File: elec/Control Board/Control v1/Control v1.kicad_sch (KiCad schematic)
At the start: 26 parts, among them J1 DB9_Female_MountingHoles, J10 Screw_Terminal_01x02, J11 Screw_Terminal_01x02, J12 Screw_Terminal_01x02, J2 Conn_01x08, J3 Conn_01x08, J4 Conn_01x08, J5 Conn_01x08, J6 Conn_01x08, J7 Conn_02x18_Odd_Even, J8 Conn_01x10_MountingPin, J9 Conn_02x12_Odd_Even

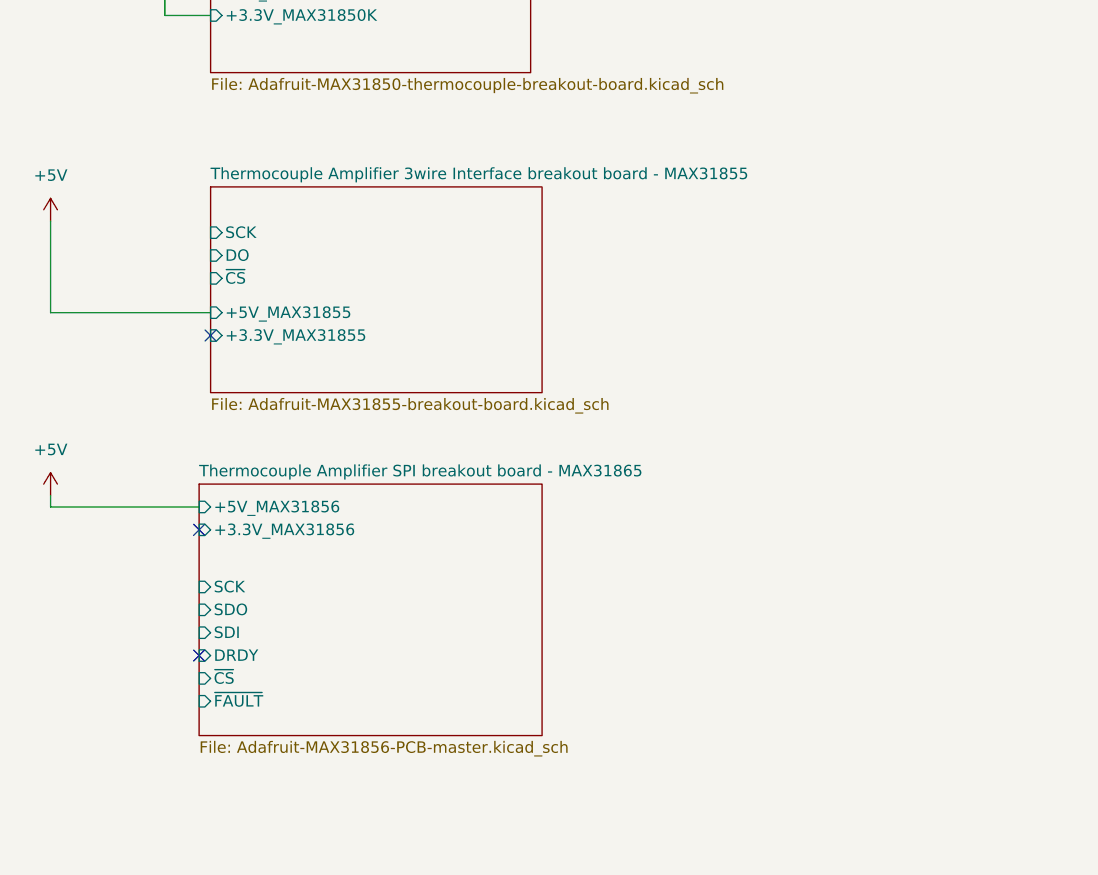
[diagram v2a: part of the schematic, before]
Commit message: Update schematic for MCP9600 I2C thermocouple.
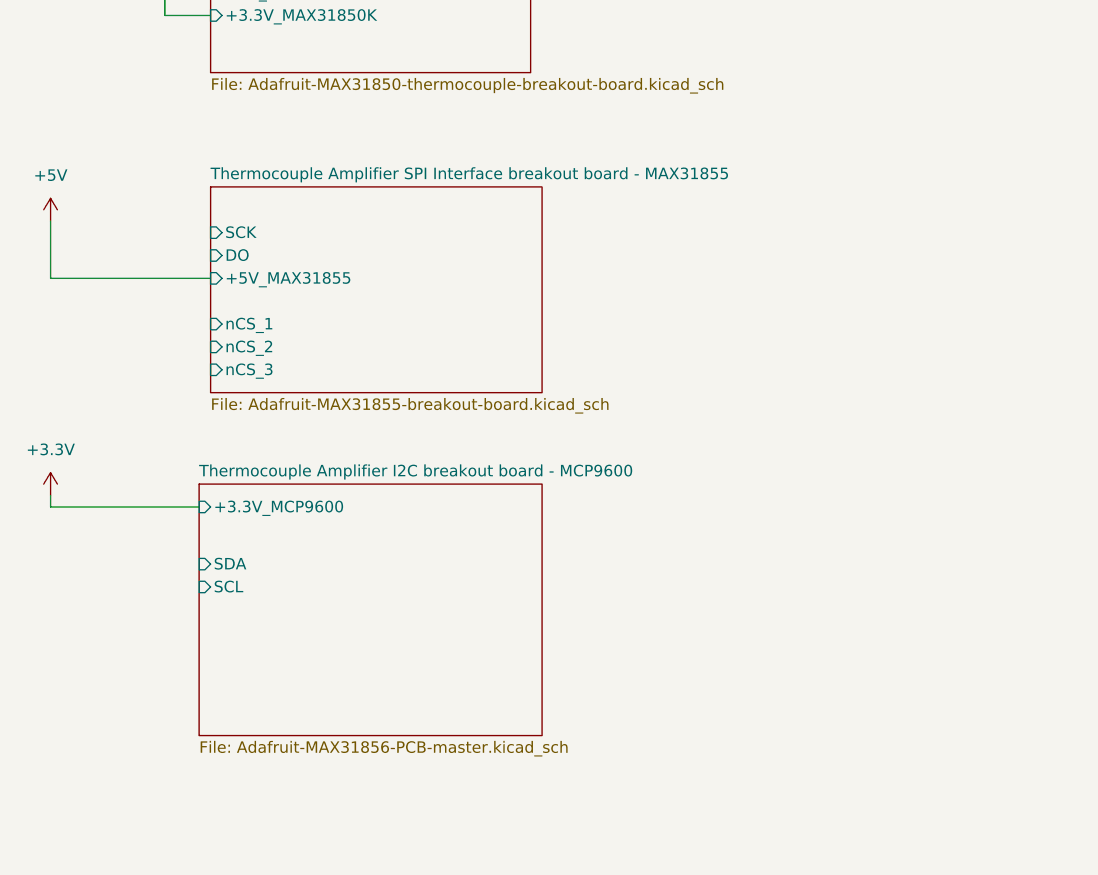
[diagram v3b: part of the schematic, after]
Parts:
- H1, H2, H3, H4, H5: footprint GeneralPurposeAlarmDevicePCB:MountingHole_3.5mm_Pad_Via -> PubInv_KiCad_PCB:MountingHole_3.5mm_Pad_Via
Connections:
- no-connect marks 9 -> 6
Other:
- sheet Thermocouple Amplifier 3wire Interface breakout board - MAX31855  renamed Thermocouple Amplifier SPI Interface breakout board - MAX31855 
- sheet Thermocouple Amplifier SPI breakout board - MAX31865 renamed Thermocouple Amplifier I2C breakout board - MCP9600
- sheet Thermocouple Amplifier I2C breakout board - MCP9600 ports: added +3.3V_MCP9600, SCL, SDA; removed +3.3V_MAX31856, +5V_MAX31856, DRDY, SCK, SDI, SDO, ~{CS}, ~{FAULT}
- sheet Thermocouple Amplifier SPI Interface breakout board - MAX31855  ports: added nCS_1, nCS_2, nCS_3; removed +3.3V_MAX31855, ~{CS}
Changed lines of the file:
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@@
   )
   (no_connect (at 29.21 166.37))
-  (no_connect (at 34.29 215.9))
   (no_connect (at 29.21 163.83))
   (no_connect (at 152.4 171.45))
   (no_connect (at 29.21 168.91))
-  (no_connect (at 33.02 251.46))
   (no_connect (at 29.21 161.29))
   (no_connect (at 29.21 171.45))
-  (no_connect (at 33.02 237.49))
   (wire (pts (xy 250.19 138.43) (xy 250.19 143.51))
     (stroke (width 0) (type default))
@@
     (stroke (width 0) (type default))
   )
-  (wire (pts (xy 34.29 213.36) (xy 16.51 213.36))
+  (wire (pts (xy 34.29 209.55) (xy 16.51 209.55))
     (stroke (width 0) (type default))
   )
@@
     (stroke (width 0) (type default))
   )
-  (wire (pts (xy 16.51 213.36) (xy 16.51 203.2))
+  (wire (pts (xy 16.51 209.55) (xy 16.51 203.2))
     (stroke (width 0) (type default))
   )
@@
       (effects (font (size 1.27 1.27)) (justify left))
     )
-    (property "Footprint" "GeneralPurposeAlarmDevicePCB:MountingHole_3.5mm_Pad_Via" (at 160.02 260.35 0)
+    (property "Footprint" "PubInv_KiCad_PCB:MountingHole_3.5mm_Pad_Via" (at 160.02 260.35 0)
       (effects (font (size 1.27 1.27)) hide)
     )
@@
       (effects (font (size 1.27 1.27)) (justify left))
     )
-    (property "Footprint" "GeneralPurposeAlarmDevicePCB:MountingHole_3.5mm_Pad_Via" (at 160.02 229.87 0)
+    (property "Footprint" "PubInv_KiCad_PCB:MountingHole_3.5mm_Pad_Via" (at 160.02 229.87 0)
       (effects (font (size 1.27 1.27)) hide)
     )
@@
       (effects (font (size 1.27 1.27)) (justify left))
     )
-    (property "Footprint" "GeneralPurposeAlarmDevicePCB:MountingHole_3.5mm_Pad_Via" (at 160.02 237.49 0)
+    (property "Footprint" "PubInv_KiCad_PCB:MountingHole_3.5mm_Pad_Via" (at 160.02 237.49 0)
       (effects (font (size 1.27 1.27)) hide)
     )
@@
     )
   )
+  (symbol (lib_id "power:+3.3V") (at 16.51 233.68 0) (mirror y) (unit 1)
+    (in_bom yes) (on_board yes) (dnp no) (fields_autoplaced)
+    (property "Reference" "#PWR028" (at 16.51 237.49 0)
+      (effects (font (size 1.27 1.27)) hide)
+    )
+    (property "Value" "+3.3V" (at 16.51 228.6 0)
+      (effects (font (size 1.27 1.27)))
+    )
+    (property "Footprint" "" (at 16.51 233.68 0)
+      (effects (font (size 1.27 1.27)) hide)
+    )
+    (property "Datasheet" "" (at 16.51 233.68 0)
+      (effects (font (size 1.27 1.27)) hide)
+    )
+    (pin "1")
+    (instances
+      (project "Control v1"
+        (path "/c68c9deb-8d4d-42f0-adf8-4d3022f4ee59"
+          (reference "#PWR028") (unit 1)
+        )
+      )
+    )
+  )
   (symbol (lib_id "Connector:Screw_Terminal_01x02") (at 394.97 194.31 0) (unit 1)
     (in_bom yes) (on_board yes) (dnp no) (fields_autoplaced)
@@
       (effects (font (size 1.27 1.27)) (justify left))
     )
-    (property "Footprint" "GeneralPurposeAlarmDevicePCB:MountingHole_3.5mm_Pad_Via" (at 160.02 252.73 0)
+    (property "Footprint" "PubInv_KiCad_PCB:MountingHole_3.5mm_Pad_Via" (at 160.02 252.73 0)
       (effects (font (size 1.27 1.27)) hide)
     )
@@
     )
   )
-  (symbol (lib_id "power:+5V") (at 16.51 233.68 0) (unit 1)
-    (in_bom yes) (on_board yes) (dnp no) (fields_autoplaced)
-    (property "Reference" "#PWR03" (at 16.51 237.49 0)
-      (effects (font (size 1.27 1.27)) hide)
-    )
-    (property "Value" "+5V" (at 16.51 228.6 0)
-      (effects (font (size 1.27 1.27)))
-    )
-    (property "Footprint" "" (at 16.51 233.68 0)
-      (effects (font (size 1.27 1.27)) hide)
-    )
-    (property "Datasheet" "" (at 16.51 233.68 0)
-      (effects (font (size 1.27 1.27)) hide)
-    )
-    (pin "1")
-    (instances
-      (project "Control v1"
-        (path "/c68c9deb-8d4d-42f0-adf8-4d3022f4ee59"
-          (reference "#PWR03") (unit 1)
-        )
-      )
-    )
-  )
   (symbol (lib_id "power:+5V") (at 16.51 203.2 0) (unit 1)
     (in_bom yes) (on_board yes) (dnp no) (fields_autoplaced)
@@
       (effects (font (size 1.27 1.27)) (justify left))
     )
-    (property "Footprint" "GeneralPurposeAlarmDevicePCB:MountingHole_3.5mm_Pad_Via" (at 160.02 245.11 0)
+    (property "Footprint" "PubInv_KiCad_PCB:MountingHole_3.5mm_Pad_Via" (at 160.02 245.11 0)
       (effects (font (size 1.27 1.27)) hide)
     )
@@
     (stroke (width 0.1524) (type solid))
     (fill (color 0 0 0 0.0000))
-    (property "Sheetname" "Thermocouple Amplifier SPI breakout board - MAX31865" (at 33.02 231.6984 0)
+    (property "Sheetname" "Thermocouple Amplifier I2C breakout board - MCP9600" (at 33.02 231.6984 0)
       (effects (font (size 1.27 1.27)) (justify left bottom))
     )
@@
       (effects (font (size 1.27 1.27)) (justify left top))
     )
-    (pin "SCK" input (at 33.02 243.84 180)
+    (pin "SDA" input (at 33.02 241.3 180)
       (effects (font (size 1.27 1.27)) (justify left))
     )
-    (pin "SDO" input (at 33.02 246.38 180)
+    (pin "SCL" input (at 33.02 243.84 180)
       (effects (font (size 1.27 1.27)) (justify left))
     )
-    (pin "SDI" input (at 33.02 248.92 180)
-      (effects (font (size 1.27 1.27)) (justify left))
-    )
-    (pin "DRDY" input (at 33.02 251.46 180)
-      (effects (font (size 1.27 1.27)) (justify left))
-    )
-    (pin "~{CS}" input (at 33.02 254 180)
-      (effects (font (size 1.27 1.27)) (justify left))
-    )
-    (pin "~{FAULT}" input (at 33.02 256.54 180)
-      (effects (font (size 1.27 1.27)) (justify left))
-    )
-    (pin "+5V_MAX31856" input (at 33.02 234.95 180)
-      (effects (font (size 1.27 1.27)) (justify left))
-    )
-    (pin "+3.3V_MAX31856" input (at 33.02 237.49 180)
+    (pin "+3.3V_MCP9600" input (at 33.02 234.95 180)
       (effects (font (size 1.27 1.27)) (justify left))
     )
@@
     (stroke (width 0.1524) (type solid))
     (fill (color 0 0 0 0.0000))
-    (property "Sheetname" "Thermocouple Amplifier 3wire Interface breakout board - MAX31855 " (at 34.29 198.6784 0)
+    (property "Sheetname" "Thermocouple Amplifier SPI Interface breakout board - MAX31855 " (at 34.29 198.6784 0)
       (effects (font (size 1.27 1.27)) (justify left bottom))
     )
@@
       (effects (font (size 1.27 1.27)) (justify left))
     )
-    (pin "~{CS}" input (at 34.29 209.55 180)
+    (pin "+5V_MAX31855" input (at 34.29 209.55 180)
+      (effects (font (size 1.27 1.27)) (justify left))
+    )
+    (pin "nCS_3" input (at 34.29 219.71 180)
       (effects (font (size 1.27 1.27)) (justify left))
     )
-    (pin "+5V_MAX31855" input (at 34.29 213.36 180)
+    (pin "nCS_2" input (at 34.29 217.17 180)
       (effects (font (size 1.27 1.27)) (justify left))
     )
-    (pin "+3.3V_MAX31855" input (at 34.29 215.9 180)
+    (pin "nCS_1" input (at 34.29 214.63 180)
       (effects (font (size 1.27 1.27)) (justify left))
     )

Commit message: Next and place thermocouple boards.
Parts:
- removed J11, J12: Screw_Terminal_01x02, symbol Connector:Screw_Terminal_01x02
- added J11 (x2): Screw_Terminal_01x02, TerminalBlock_TE-Connectivity:TerminalBlock_TE_282834-2_1x02_P2.54mm_Horizontal, symbol Connector:Screw_Terminal_01x02
- added S101: SWITCH_TACTILE_SPST-NO_0.05A_24V, PubInv_KiCad_PCB:Switch_Tactile_THT_6x6mm, symbol GPAD_SCH_LIB:SWITCH_TACTILE_SPST-NO_0.05A_24V
- added TP103: Due_5V2, TestPoint:TestPoint_Loop_D2.54mm_Drill1.5mm_Beaded, symbol Connector:TestPoint
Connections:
- net +24V: now also J11.1 (Pin_1)
- net GND: now also A1.GND4 (SPI_GND), J11.2 (Pin_2), S101.1, S101.2
- net SSR Interface/Heater_SSR_High: now also J11.1 (Pin_1)
- net SSR Interface/Heater_SSR_Low: now also J11.2 (Pin_2)
- net at A1.5V2 (SPI_5V): now also TP103.1
- net at A1.RST2 (SPI_RESET): now also S101.3, S101.4
- no-connect marks 6 -> 1
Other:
- sheet Thermocouple Amplifier with 1-Wire Breakout Board - MAX31850K ports: added none; removed +3.3V_MAX31850K, A0, A1, A2, A3

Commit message: Fix swome ERC errors.
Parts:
- removed J8: Conn_01x10_MountingPin, Connector_PinSocket_2.54mm:PinSocket_1x10_P2.54mm_Vertical, symbol Connector_Generic_MountingPin:Conn_01x10_MountingPin
- added J14: Conn_01x08, symbol Connector_Generic:Conn_01x08
- added J8, J9: Conn_01x10, Connector_PinSocket_2.54mm:PinSocket_1x10_P2.54mm_Vertical, symbol Connector_Generic:Conn_01x10
- added R101 (x7): 1R0, Resistor_SMD:R_0603_1608Metric_Pad0.98x0.95mm_HandSolder, symbol Device:R
- added R301: 1R, Resistor_SMD:R_0603_1608Metric_Pad0.98x0.95mm_HandSolder, symbol Device:R
- renumbered J9 to J10, J10 to J11
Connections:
- net ACI: now also J9.7 (Pin_7)
- net AREF: now also J8.3 (Pin_3)
- net AUX: now also J14.6 (Pin_6), J9.10 (Pin_10), J9.9 (Pin_9)
- net BLOWER_PWM: now also J8.9 (Pin_9)
- net COPI: now also R101.1
- net EN+: now also J9.6 (Pin_6)
- net EN-: now also J9.5 (Pin_5)
- net GND: now also J14.3 (Pin_3), J14.5 (Pin_5), J14.7 (Pin_7), J14.8 (Pin_8), J8.4 (Pin_4)
- net PAR: now also J9.4 (Pin_4)
- net POK: now also J9.3 (Pin_3)
- net SCL: now also R101.1
- net SCL1: now also J8.1 (Pin_1)
- net SDA: now also R101.1
- net SDA1: now also J8.2 (Pin_2)
- net SPI_SCK: now also R101.1
- net SSR Interface/Heater: now also R301.2
- net Thermocouple Amplifier I2C breakout board - MCP9600/SCL: now also R101.2
- net Thermocouple Amplifier I2C breakout board - MCP9600/SDA: now also R101.2
- net Thermocouple Amplifier SPI Interface breakout board - MAX31855 /DO: now also R101.2
- net Thermocouple Amplifier SPI Interface breakout board - MAX31855 /SCK: now also R101.2
- net Thermocouple Amplifier SPI Interface breakout board - MAX31855 /nCS_1: now also R101.2
- net Thermocouple Amplifier SPI Interface breakout board - MAX31855 /nCS_2: now also R101.2
- net Thermocouple Amplifier SPI Interface breakout board - MAX31855 /nCS_3: now also R101.2
- net VCI: now also J9.8 (Pin_8)
- net VO+: now also J14.1 (Pin_1)
- net VO-: now also J14.2 (Pin_2)
- net VS+: now also J9.1 (Pin_1)
- net VS-: now also J9.2 (Pin_2)
- net VSET: now also J14.4 (Pin_4)
- net at A1.D10 (D10_CS0): now also J8.8 (Pin_8)
- net at A1.D11: now also J8.7 (Pin_7)
- net at A1.D12: now also J8.6 (Pin_6)
- net at A1.D13: now also J8.5 (Pin_5)
- net at A1.D8: now also J8.10 (Pin_10)
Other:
- sheet I2C_LevelShift ports: added +12forSPIPeripherial, +3V3LevelShift, +5LevelShift; removed none
- moved on the sheet: R101

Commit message: Place PCB components.
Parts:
- added C301 (x2): 39PF, Capacitor_SMD:C_0603_1608Metric_Pad1.08x0.95mm_HandSolder, symbol Device:C
- added R101 (x3): 1R0, Resistor_SMD:R_0603_1608Metric_Pad0.98x0.95mm_HandSolder, symbol Device:R
- added TP103: TX, TestPoint:TestPoint_Loop_D2.54mm_Drill1.5mm_Beaded, symbol Connector:TestPoint
- added TP103: RX, TestPoint:TestPoint_Loop_D2.54mm_Drill1.5mm_Beaded, symbol Connector:TestPoint
- J11: footprint (none) -> TerminalBlock_TE-Connectivity:TerminalBlock_TE_282834-2_1x02_P2.54mm_Horizontal; AssemblyType (none) -> HAND; Cost (none) -> 0.1537; Distributor 1 (none) -> JLCPCB; Distributor 1 PN (none) -> C2915639
- J14: footprint (none) -> Connector_PinSocket_2.54mm:PinSocket_1x10_P2.54mm_Vertical
- renumbered J4 to J2, J2 to J3, J3 to J4
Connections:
- net +12V: now also A1.VIN, J2.1 (Pin_1)
- net +5V: now also A1.5V3 (5V), A1.5V4 (5V)
- net 5V3: no longer A1.5V3 (5V)
- net 5V4: no longer A1.5V4 (5V)
- net D33: now also R101.1
- net D35: now also J1.1, R101.1, C301.1, R101.2
- net D51: now also R301.1
- net D_PSU_RX: now also R101.2, TP103.1; no longer J10.23 (Pin_23)
- net D_PSU_TX: now also R101.1, TP103.1; no longer J10.24 (Pin_24)
- net GND: now also C301.2, C301.2
- net D34: now reaches A1.D34, J7.15 (Pin_15)
- net D34: now also R101.1
- net at J1.5: now also C301.1, R101.1
- new net RX: J10.24 (Pin_24), R101.2
- new net TX: J10.23 (Pin_23), R101.1
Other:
- note added: "Due Pin Number Connection Notes * A0 Blower Tachometer * D4 Dallas One-Wire connection to Thermocouple Breakouts * D9 Blower PWM ??? D18 Digital Power Supply TF800 Pin 23 This is Serial1 TX https://assets.alliedelec.com/v1560852133/Datasheets/1d230174086e96b6e4801d1c963649f3.pdf ??? D19 Digital Power Supply TF800 Pin 24 This is Serial1 RX https://assets.alliedelec.com/v1560852133/Datasheets/1d230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"
- note removed: "Due Pin Number Connection Notes A0 Blower Tachometer D4 Dallas One-Wire connection to Thermocouple Breakouts D9 Blower PWM D18 Digital Power Supply TF800 Pin 23 This is Serial1 TX https://assets.alliedelec.com/v1560852133/Datasheets/1d230174086e96b6e4801d1c963649f3.pdf D19 Digital Power Supply TF800 Pin 24 This is Serial1 RX https://assets.alliedelec.com/v1560852133/Datasheets/1d230174086e96b6e48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"
- moved on the sheet: J1, J11, J2, J3, J7, R101, S101
